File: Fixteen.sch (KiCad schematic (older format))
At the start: 9 parts, among them J1 TED_SOCKET, J2 CAS_EXT_CONN, J98 KICAD_LOGO, J99 OSHW_LOGO, U1 MOS_7360_TED, U2 74LS253

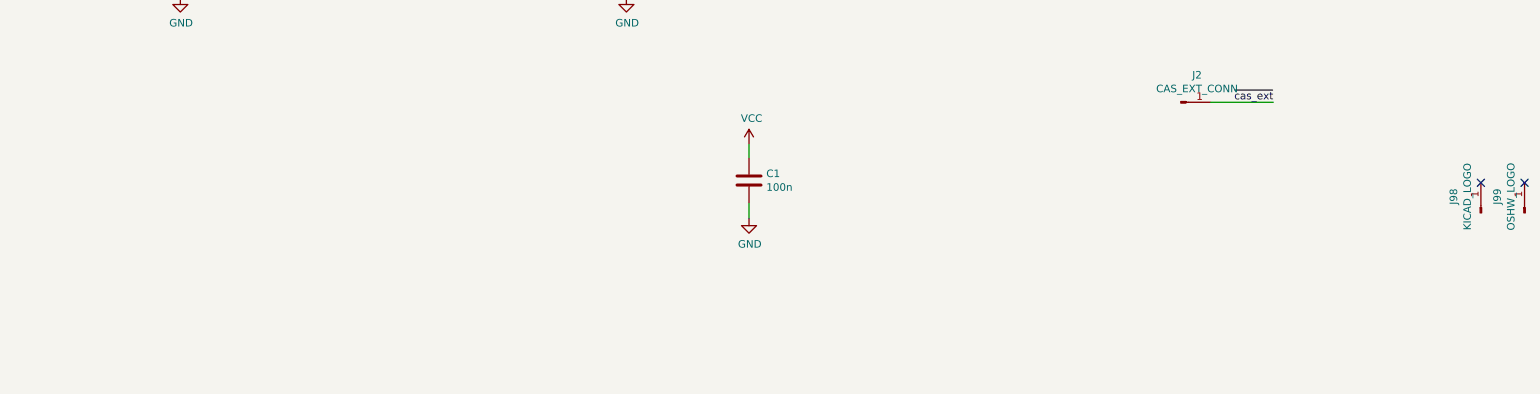
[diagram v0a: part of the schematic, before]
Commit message: Add ESD protection (?) Found all of this stuff uncommitted after months... :|
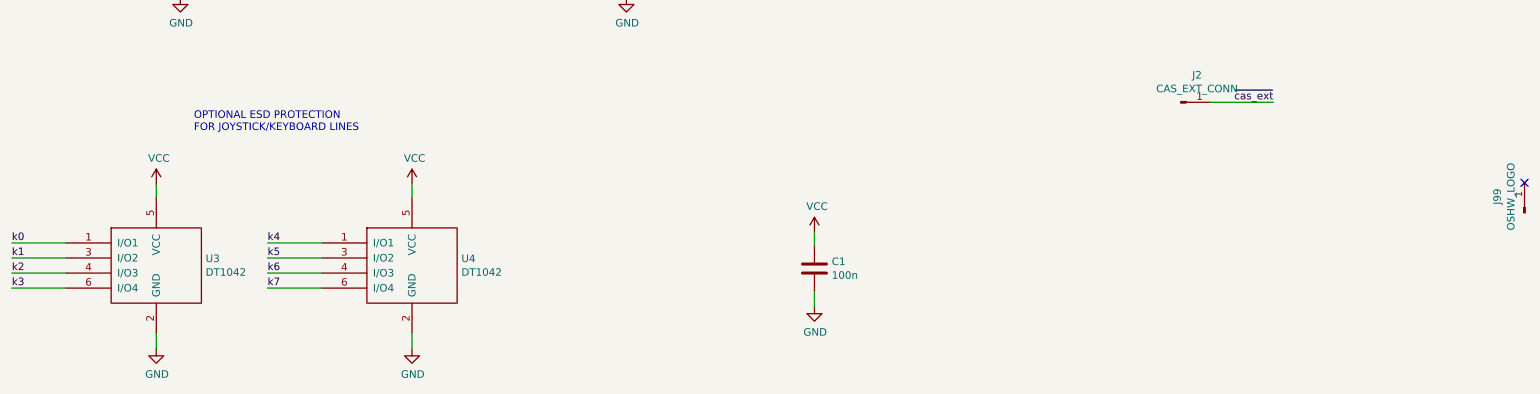
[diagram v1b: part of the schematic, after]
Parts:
- removed J98: KICAD_LOGO, Symbol:KiCad-Logo2_6mm_Copper, symbol Connector:Conn_01x01_Male
- added U3, U4: DT1042, Package_SO:TSOP-6_1.65x3.05mm_P0.95mm, symbol DT1042:DT1042
- J1: footprint Package_DIP:DIP-48_W15.24mm_LongPads -> Fixteen:DIP-48_W15.24mm_LongPads_ModSilkS
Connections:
- net GND: now also U3.2 (GND), U4.2 (GND)
- net VCC: now also U3.5 (VCC), U4.5 (VCC)
- net k0: now also U3.1 (I/O1)
- net k1: now also U3.3 (I/O2)
- net k2: now also U3.4 (I/O3)
- net k3: now also U3.6 (I/O4)
- net k4: now also U4.1 (I/O1)
- net k5: now also U4.3 (I/O2)
- net k6: now also U4.4 (I/O3)
- net k7: now also U4.6 (I/O4)
- no-connect marks 2 -> 1
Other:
- note added: "OPTIONAL ESD PROTECTION\nFOR JOYSTICK/KEYBOARD LINES"
- moved on the sheet: C1
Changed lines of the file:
@@
 Sheet 1 1
 Title "Fixteen"
-Date "2019-11-22"
+Date "2019-11-24"
 Rev "1git"
 Comp "SukkoPera"
@@
 F 0 "J1" H 6380 5015 50  0000 C CNN
 F 1 "TED_SOCKET" H 6380 4924 50  0000 C CNN
-F 2 "Package_DIP:DIP-48_W15.24mm_LongPads" H 6380 3500 50  0001 C CNN
+F 2 "Fixteen:DIP-48_W15.24mm_LongPads_ModSilkS" H 6380 3500 50  0001 C CNN
 F 3 "DOCUMENTATION" H 6380 3500 50  0001 C CNN
 	1    6380 3500
@@
 L power:VCC #PWR07
 U 1 1 5DED441F
-P 5905 5895
-F 0 "#PWR07" H 5905 5745 50  0001 C CNN
-F 1 "VCC" H 5922 6068 50  0000 C CNN
-F 2 "" H 5905 5895 50  0001 C CNN
-F 3 "" H 5905 5895 50  0001 C CNN
-	1    5905 5895
+P 6340 6480
+F 0 "#PWR07" H 6340 6330 50  0001 C CNN
+F 1 "VCC" H 6357 6653 50  0000 C CNN
+F 2 "" H 6340 6480 50  0001 C CNN
+F 3 "" H 6340 6480 50  0001 C CNN
+	1    6340 6480
 	1    0    0    -1
 $EndComp
@@
 L power:GND #PWR08
 U 1 1 5DED49CF
-P 5905 6385
-F 0 "#PWR08" H 5905 6135 50  0001 C CNN
-F 1 "GND" H 5910 6212 50  0000 C CNN
-F 2 "" H 5905 6385 50  0001 C CNN
-F 3 "" H 5905 6385 50  0001 C CNN
-	1    5905 6385
+P 6340 6970
+F 0 "#PWR08" H 6340 6720 50  0001 C CNN
+F 1 "GND" H 6345 6797 50  0000 C CNN
+F 2 "" H 6340 6970 50  0001 C CNN
+F 3 "" H 6340 6970 50  0001 C CNN
+	1    6340 6970
 	1    0    0    -1
 $EndComp
@@
 L Device:C C1
 U 1 1 5DED5243
-P 5905 6135
-F 0 "C1" H 6020 6181 50  0000 L CNN
-F 1 "100n" H 6020 6090 50  0000 L CNN
-F 2 "Capacitor_SMD:C_0805_2012Metric_Pad1.15x1.40mm_HandSolder" H 5943 5985 50  0001 C CNN
-F 3 "~" H 5905 6135 50  0001 C CNN
-	1    5905 6135
-	1    0    0    -1
-$EndComp
-Wire Wire Line
-	5905 5895 5905 5985
-Wire Wire Line
-	5905 6385 5905 6285
+P 6340 6720
+F 0 "C1" H 6455 6766 50  0000 L CNN
+F 1 "100n" H 6455 6675 50  0000 L CNN
+F 2 "Capacitor_SMD:C_0805_2012Metric_Pad1.15x1.40mm_HandSolder" H 6378 6570 50  0001 C CNN
+F 3 "~" H 6340 6720 50  0001 C CNN
+	1    6340 6720
+	1    0    0    -1
+$EndComp
+Wire Wire Line
+	6340 6480 6340 6570
+Wire Wire Line
+	6340 6970 6340 6870
 $Comp
 L Connector:Conn_01x01_Male J99
@@
 NoConn ~ 11060 6150
 $Comp
-L Connector:Conn_01x01_Male J98
-U 1 1 5DF12BDC
-P 10770 6350
-F 0 "J98" H 10878 6531 50  0000 C CNN
-F 1 "KICAD_LOGO" H 10878 6440 50  0000 C CNN
-F 2 "Symbol:KiCad-Logo2_6mm_Copper" H 10770 6350 50  0001 C CNN
-F 3 "~" H 10770 6350 50  0001 C CNN
-	1    10770 6350
-	0    -1   -1   0
-$EndComp
-NoConn ~ 10770 6150
+L DT1042:DT1042 U3
+U 1 1 5DF30E82
+P 1965 6700
+F 0 "U3" H 2293 6746 50  0000 L CNN
+F 1 "DT1042" H 2293 6655 50  0000 L CNN
+F 2 "Package_SO:TSOP-6_1.65x3.05mm_P0.95mm" H 1965 6700 50  0001 C CNN
+F 3 "" H 1965 6700 50  0001 C CNN
+	1    1965 6700
+	1    0    0    -1
+$EndComp
+$Comp
+L power:VCC #PWR09
+U 1 1 5DF3BE45
+P 1965 6160
+F 0 "#PWR09" H 1965 6010 50  0001 C CNN
+F 1 "VCC" H 1982 6333 50  0000 C CNN
+F 2 "" H 1965 6160 50  0001 C CNN
+F 3 "" H 1965 6160 50  0001 C CNN
+	1    1965 6160
+	1    0    0    -1
+$EndComp
+Wire Wire Line
+	1965 6160 1965 6250
+$Comp
+L power:GND #PWR010
+U 1 1 5DF4C28D
+P 1965 7250
+F 0 "#PWR010" H 1965 7000 50  0001 C CNN
+F 1 "GND" H 1970 7077 50  0000 C CNN
+F 2 "" H 1965 7250 50  0001 C CNN
+F 3 "" H 1965 7250 50  0001 C CNN
+	1    1965 7250
+	1    0    0    -1
+$EndComp
+Wire Wire Line
+	1965 7250 1965 7150
+Text Label 1005 6850 0    50   ~ 0
+k3
+Text Label 1005 6750 0    50   ~ 0
+k2
+Text Label 1005 6650 0    50   ~ 0
+k1
+Text Label 1005 6550 0    50   ~ 0
+k0
+Wire Wire Line
+	1365 6850 1005 6850
+Wire Wire Line
+	1365 6750 1005 6750
+Wire Wire Line
+	1365 6650 1005 6650
+Wire Wire Line
+	1365 6550 1005 6550
+Text Label 2705 6550 0    50   ~ 0
+k4
+Text Label 2705 6650 0    50   ~ 0
+k5
+Text Label 2705 6750 0    50   ~ 0
+k6
+Text Label 2705 6850 0    50   ~ 0
+k7
+Text Notes 2215 5815 0    50   ~ 0
+OPTIONAL ESD PROTECTION\nFOR JOYSTICK/KEYBOARD LINES
+Wire Wire Line
+	3065 6850 2705 6850
+Wire Wire Line
+	3065 6750 2705 6750
+Wire Wire Line
+	3065 6650 2705 6650
+Wire Wire Line
+	3065 6550 2705 6550
+Wire Wire Line
+	3665 7250 3665 7150
+$Comp
+L power:GND #PWR012
+U 1 1 5DF43F9D
+P 3665 7250
+F 0 "#PWR012" H 3665 7000 50  0001 C CNN
+F 1 "GND" H 3670 7077 50  0000 C CNN
+F 2 "" H 3665 7250 50  0001 C CNN
+F 3 "" H 3665 7250 50  0001 C CNN
+	1    3665 7250
+	1    0    0    -1
+$EndComp
+Wire Wire Line
+	3665 6160 3665 6250
+$Comp
+L power:VCC #PWR011
+U 1 1 5DF33F13
+P 3665 6160
+F 0 "#PWR011" H 3665 6010 50  0001 C CNN
+F 1 "VCC" H 3682 6333 50  0000 C CNN
+F 2 "" H 3665 6160 50  0001 C CNN
+F 3 "" H 3665 6160 50  0001 C CNN
+	1    3665 6160
+	1    0    0    -1
+$EndComp
+$Comp
+L DT1042:DT1042 U4
+U 1 1 5DF319FC
+P 3665 6700
+F 0 "U4" H 3993 6746 50  0000 L CNN
+F 1 "DT1042" H 3993 6655 50  0000 L CNN
+F 2 "Package_SO:TSOP-6_1.65x3.05mm_P0.95mm" H 3665 6700 50  0001 C CNN
+F 3 "" H 3665 6700 50  0001 C CNN
+	1    3665 6700
+	1    0    0    -1
+$EndComp
 $EndSCHEMATC

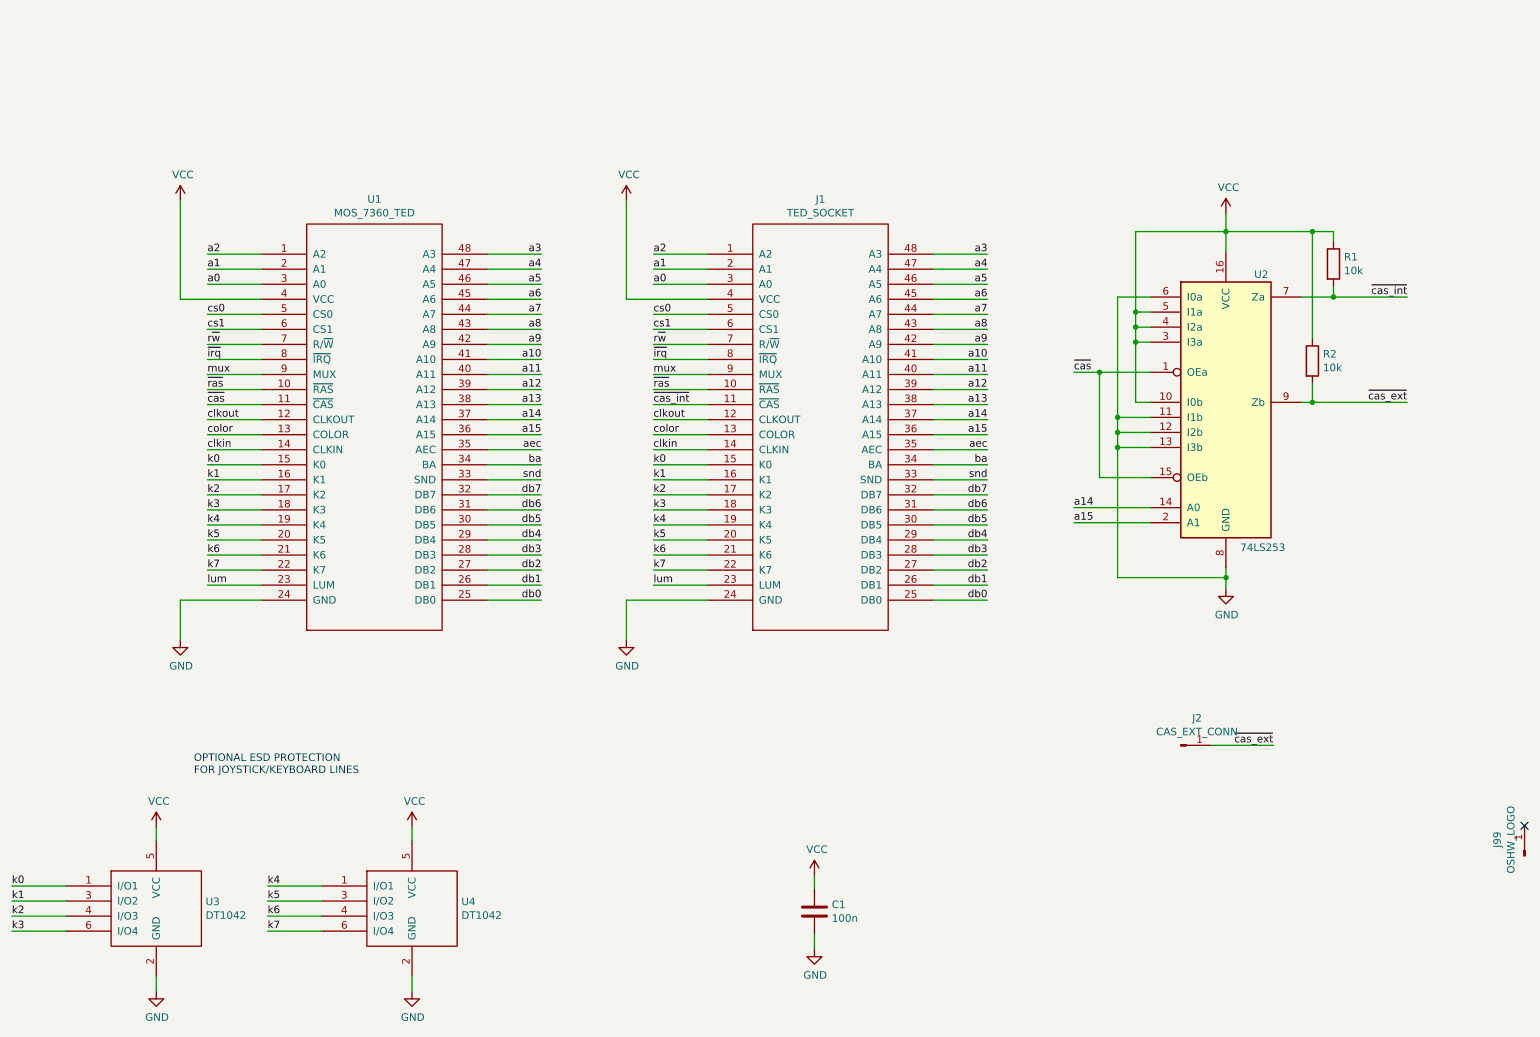
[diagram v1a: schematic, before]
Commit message: Turned this into a ESD protection + 64k internal RAM expansion
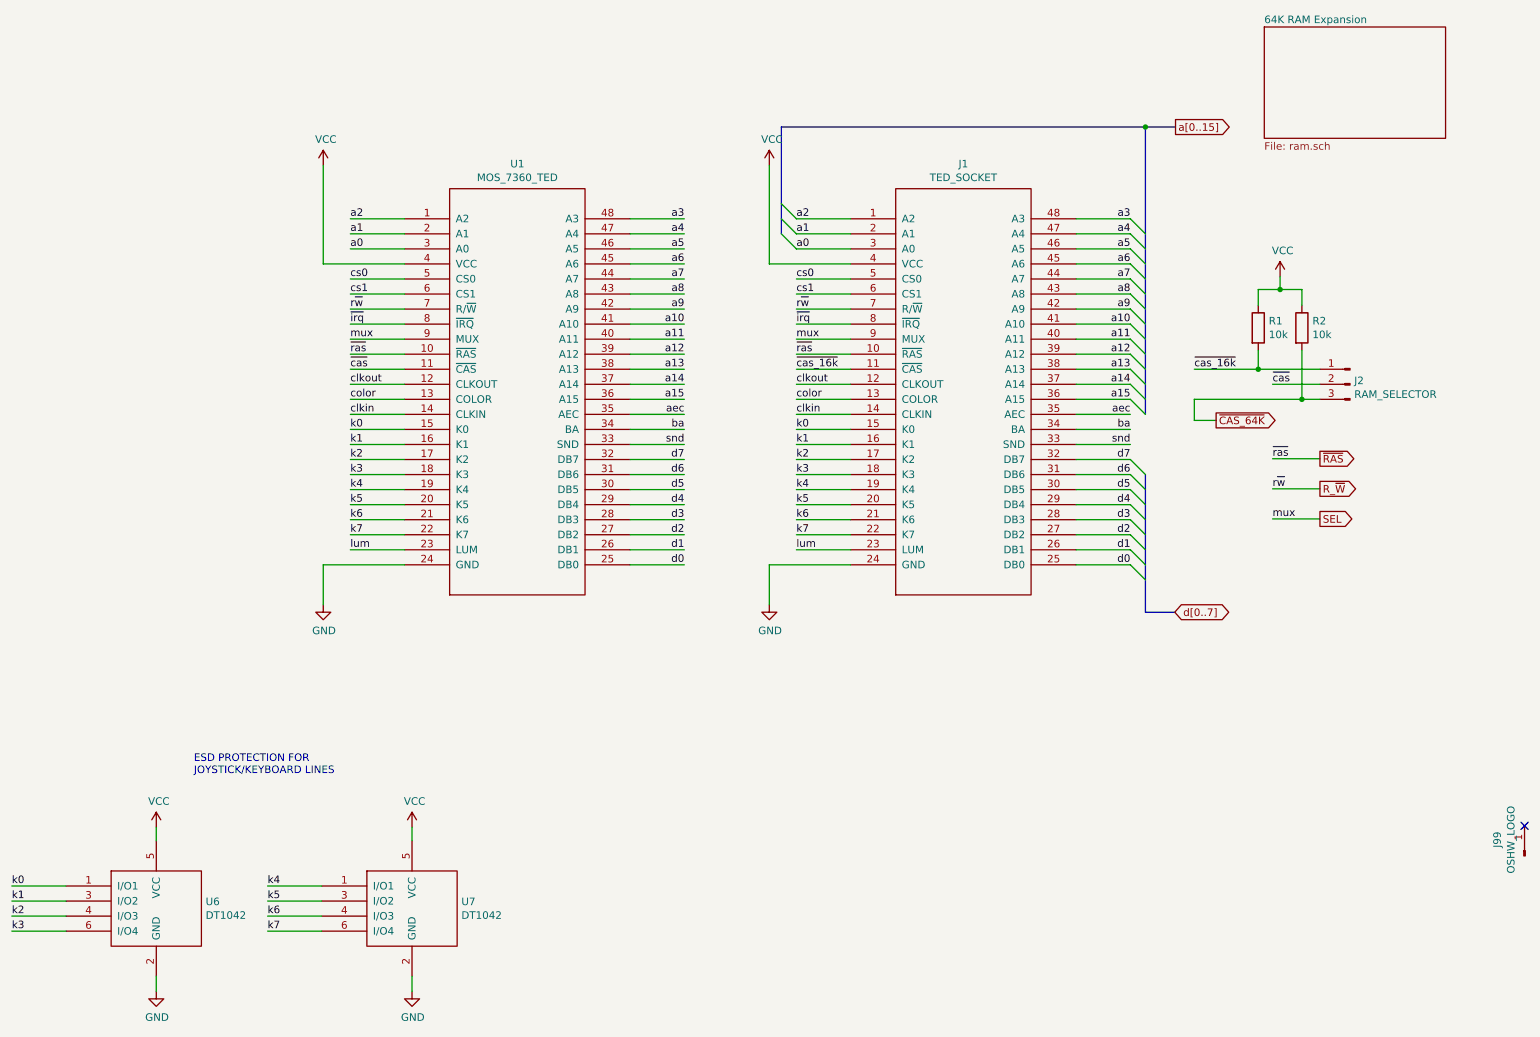
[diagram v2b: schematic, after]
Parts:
- removed C1: 100n, Capacitor_SMD:C_0805_2012Metric_Pad1.15x1.40mm_HandSolder, symbol Device:C
- removed J2: CAS_EXT_CONN, Fixteen:PinHeader_1x01_P2.54mm_Vertical, symbol Connector:Conn_01x01_Male
- removed U2: 74LS253, Package_SO:SOIC-16_3.9x9.9mm_P1.27mm, symbol 74xx:74LS253
- added J2: RAM_SELECTOR, Fixteen:Pin_Header_Straight_1x03-ModSilkS, symbol Connector:Conn_01x03_Male
- R1, R2: footprint Resistor_SMD:R_0805_2012Metric_Pad1.15x1.40mm_HandSolder -> Resistor_SMD:R_0805_2012Metric_Pad1.20x1.40mm_HandSolder
- renumbered U3 to U6, U4 to U7
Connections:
- net ~cas: now also J2.2 (Pin_2)
- net db0 renamed d0
- net db1 renamed d1
- net db2 renamed d2
- net db3 renamed d3
- net db4 renamed d4
- net db5 renamed d5
- net db6 renamed d6
- net db7 renamed d7
- net mux renamed SEL
- net r~w renamed R_~W
- net ~cas_ext renamed ~CAS_64K
- net ~CAS_64K: now also J2.3 (Pin_3)
- net ~cas_int renamed ~cas_16k
- net ~cas_16k: now also J2.1 (Pin_1)
- net ~ras renamed ~RAS
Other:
- note added: "ESD PROTECTION FOR\nJOYSTICK/KEYBOARD LINES"
- note removed: "OPTIONAL ESD PROTECTION\nFOR JOYSTICK/KEYBOARD LINES"
- moved on the sheet: J1, U1

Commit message: Finalize release
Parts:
- J99: footprint Symbol:OSHW-Logo_7.5x8mm_Copper -> Symbol:OSHW-Logo_5.7x6mm_Copper; LCSC (none) -> -; MouserPN (none) -> -
- R1, R2: LCSC (none) -> C17414
- U6, U7: LCSC (none) -> C460064; MouserPN (none) -> 621-DT1042-04TS-7; Notes (none) -> Optional, for TED ESD protection through joystick port
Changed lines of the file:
@@
 F 0 "J99" H 11168 6531 50  0000 C CNN
 F 1 "OSHW_LOGO" H 11168 6440 50  0000 C CNN
-F 2 "Symbol:OSHW-Logo_7.5x8mm_Copper" H 11060 6350 50  0001 C CNN
+F 2 "Symbol:OSHW-Logo_5.7x6mm_Copper" H 11060 6350 50  0001 C CNN
 F 3 "~" H 11060 6350 50  0001 C CNN
+F 4 "-" H 11060 6350 50  0001 C CNN "LCSC"
+F 5 "-" H 11060 6350 50  0001 C CNN "MouserPN"
 	1    11060 6350
 	0    -1   -1   0
@@
 F 2 "Package_SO:TSOP-6_1.65x3.05mm_P0.95mm" H 1965 6700 50  0001 C CNN
 F 3 "" H 1965 6700 50  0001 C CNN
+F 4 "C460064" H 1965 6700 50  0001 C CNN "LCSC"
+F 5 "621-DT1042-04TS-7" H 1965 6700 50  0001 C CNN "MouserPN"
+F 6 "Optional, for TED ESD protection through joystick port" H 1965 6700 50  0001 C CNN "Notes"
 	1    1965 6700
 	1    0    0    -1
@@
 F 2 "Package_SO:TSOP-6_1.65x3.05mm_P0.95mm" H 3665 6700 50  0001 C CNN
 F 3 "" H 3665 6700 50  0001 C CNN
+F 4 "C460064" H 3665 6700 50  0001 C CNN "LCSC"
+F 5 "621-DT1042-04TS-7" H 3665 6700 50  0001 C CNN "MouserPN"
+F 6 "Optional, for TED ESD protection through joystick port" H 3665 6700 50  0001 C CNN "Notes"
 	1    3665 6700
 	1    0    0    -1
@@
 F 2 "Resistor_SMD:R_0805_2012Metric_Pad1.20x1.40mm_HandSolder" V 9510 2840 50  0001 C CNN
 F 3 "~" H 9580 2840 50  0001 C CNN
+F 4 "C17414" H 9580 2840 50  0001 C CNN "LCSC"
 	1    9580 2840
 	1    0    0    -1
@@
 F 2 "Resistor_SMD:R_0805_2012Metric_Pad1.20x1.40mm_HandSolder" V 9220 2840 50  0001 C CNN
 F 3 "~" H 9290 2840 50  0001 C CNN
+F 4 "C17414" H 9290 2840 50  0001 C CNN "LCSC"
 	1    9290 2840
 	1    0    0    -1
